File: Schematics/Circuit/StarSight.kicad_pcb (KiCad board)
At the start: 2 copper layers, 21 parts, among them J10 IR1, J11 IR1, J12 ultSound1, J13 ultSound1, J14 ultSound1, J15 ultSound1, J2 Line1, J3 Line2, J4 Line3, J5 Line4, J6 Line5, J7 IR1, J8 IR1, J9 IR1, P1 CONN_13X2, P2 Power, U1 LM1084IT-5.0/NOPB

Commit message: Fix pcb
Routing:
- added copper zone on F.Cu, net GND

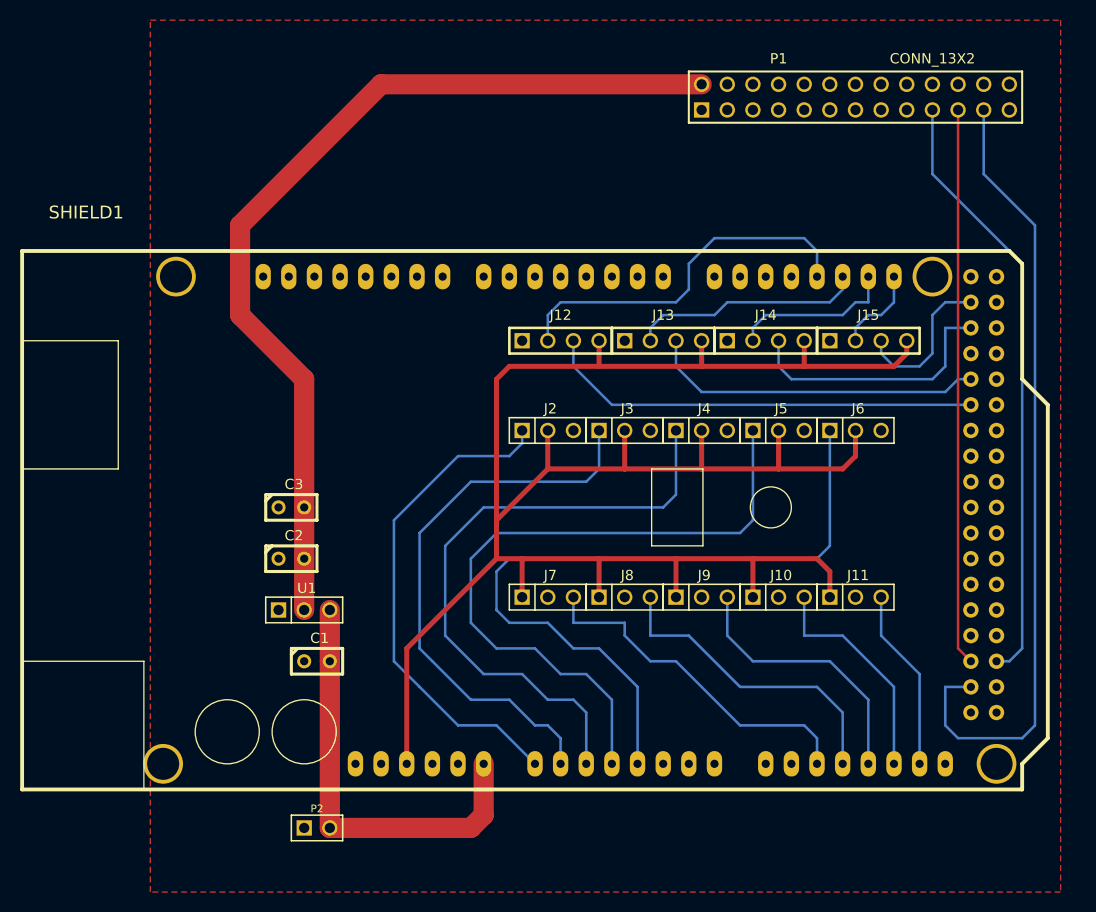
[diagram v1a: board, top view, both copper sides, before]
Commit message: Edit board - remove drivers, add pins
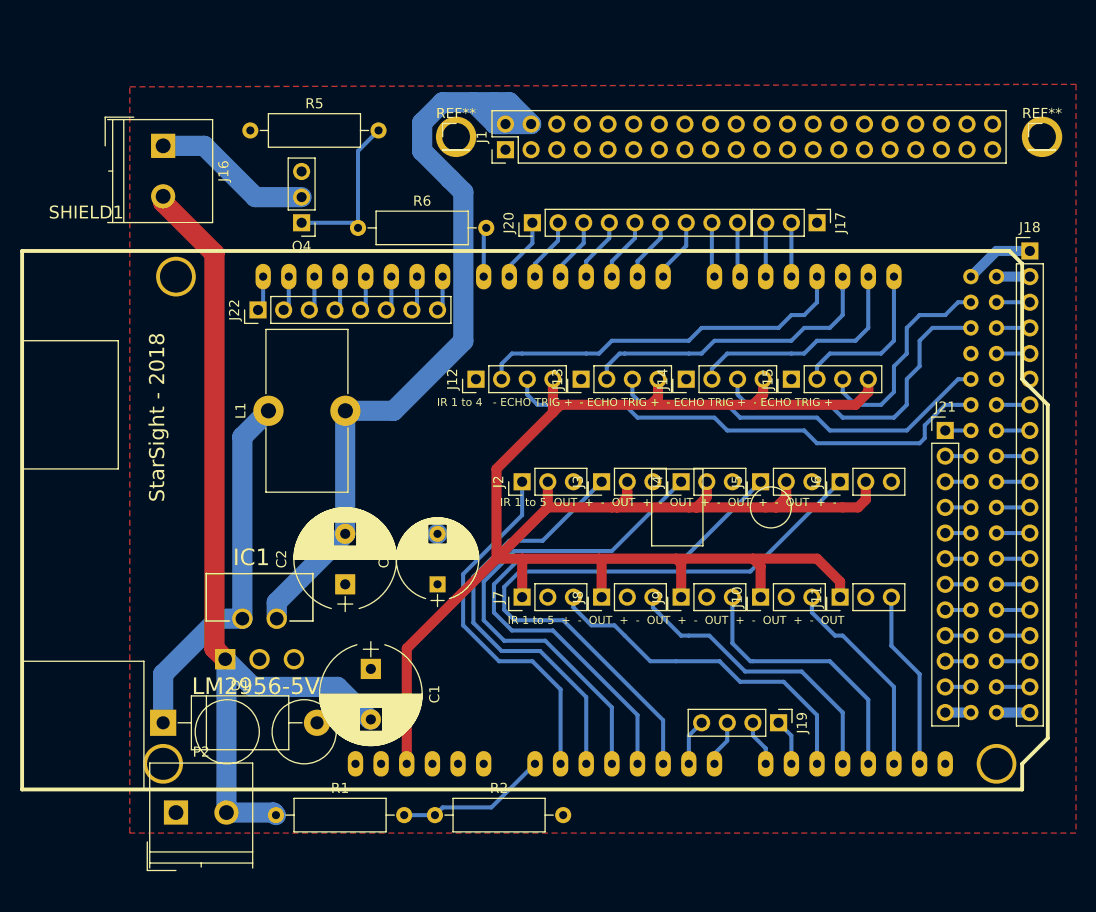
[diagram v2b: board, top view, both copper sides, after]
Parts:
- removed P1: CONN_13X2, pin_array_13x2
- removed U1: LM1084IT-5.0/NOPB, PIN_ARRAY_3X1
- added D1: 1n5824, Diodes_THT:D_DO-201_P15.24mm_Horizontal, F.Cu at (116.8, 111.5)
- added IC1: LM2956-5V, reg:TO170P470X1016X2092-5P, F.Cu at (129.8, 93.0)
- added J1: Conn_02x20_Odd_Even, Pin_Headers:Pin_Header_Straight_2x20_Pitch2.54mm, F.Cu at (150.7, 54.7)
- added J16: Conn_01x02, Connectors_Terminal_Blocks:TerminalBlock_Philmore_TB132_02x5mm_Straight, F.Cu at (116.8, 54.4)
- added J17: Conn_01x03, Pin_Headers:Pin_Header_Straight_1x03_Pitch2.54mm, F.Cu at (181.6, 62.0)
- added J18: Conn_01x19, Pin_Headers:Pin_Header_Straight_1x19_Pitch2.54mm, F.Cu at (202.7, 64.8)
- added J19: Conn_01x04, Pin_Headers:Pin_Header_Straight_1x04_Pitch2.54mm, F.Cu at (177.8, 111.5)
- added J20: Conn_01x09, Pin_Headers:Pin_Header_Straight_1x09_Pitch2.54mm, F.Cu at (153.4, 62.0)
- added J21: Conn_01x12, Pin_Headers:Pin_Header_Straight_1x12_Pitch2.54mm, F.Cu at (194.3, 82.5)
- added J22: Conn_01x08, Pin_Headers:Pin_Header_Straight_1x08_Pitch2.54mm, F.Cu at (126.2, 70.6)
- added L1: 33 uH, Inductors_THT:L_Toroid_Vertical_L16.0mm_W8.0mm_P7.62mm, F.Cu at (127.3, 80.6)
- added Q4: BUZZ TO220, Pin_Headers:Pin_Header_Straight_1x03_Pitch2.54mm, F.Cu at (130.6, 62.0)
- added R1: 20k, Resistors_THT:R_Axial_DIN0309_L9.0mm_D3.2mm_P12.70mm_Horizontal, F.Cu at (128.0, 120.7)
- added R2: 10k, Resistors_THT:R_Axial_DIN0309_L9.0mm_D3.2mm_P12.70mm_Horizontal, F.Cu at (143.8, 120.7)
- added R5: 10k, Resistors_THT:R_Axial_DIN0309_L9.0mm_D3.2mm_P12.70mm_Horizontal, F.Cu at (125.5, 52.8)
- added R6: 100, Resistors_THT:R_Axial_DIN0309_L9.0mm_D3.2mm_P12.70mm_Horizontal, F.Cu at (136.1, 62.5)
- added REF**: Pin_Header_Straight_1x01_Pitch2.54mm, Pin_Headers:Pin_Header_Straight_1x01_Pitch2.54mm, F.Cu at (203.9, 53.5)
- added REF**: Pin_Header_Straight_1x01_Pitch2.54mm, Pin_Headers:Pin_Header_Straight_1x01_Pitch2.54mm, F.Cu at (145.9, 53.5)
- C1: value 10 uF -> 220 uF; footprint C1 -> Capacitors_THT:CP_Radial_D10.0mm_P5.00mm
- C2: value 10 uF -> 680 uF; footprint C1 -> Capacitors_THT:CP_Radial_D10.0mm_P5.00mm
- C3: footprint C1 -> Capacitors_THT:CP_Radial_D8.0mm_P5.00mm
- J10, J11, J2, J3, J4, J5, J6, J7, J8, J9: footprint PIN_ARRAY_3X1 -> Pin_Headers:Pin_Header_Straight_1x03_Pitch2.54mm
- J12, J13, J14, J15: footprint PIN_ARRAY_4x1 -> Pin_Headers:Pin_Header_Straight_1x04_Pitch2.54mm
- P2: footprint PIN_ARRAY_2X1 -> Connectors_Terminal_Blocks:TerminalBlock_Philmore_TB132_02x5mm_Straight
- SHIELD1: footprint ARDUINO_MEGA_SHIELD -> arduino_shields:ARDUINO_MEGA_SHIELD
- moved C3 16.4 mm to (144.0, 97.8), turned to 90 degrees
- moved P2 14.1 mm to (118.1, 120.4)
- moved J12 9.21 mm to (147.8, 77.5), turned to 90 degrees
- moved J13 8.98 mm to (158.2, 77.5), turned to 90 degrees
- moved J14 8.75 mm to (168.7, 77.5), turned to 90 degrees
- moved J15 8.52 mm to (179.1, 77.5), turned to 90 degrees
- moved C2 5.91 mm to (134.9, 97.8), turned to 90 degrees
- moved J2 5.68 mm to (152.4, 87.6), turned to 90 degrees
- moved J3 5.57 mm to (160.3, 87.6), turned to 90 degrees
- moved J4 5.47 mm to (168.1, 87.6), turned to 90 degrees
- moved C1 5.39 mm to (137.4, 106.2), turned to 270 degrees
- moved J5 5.38 mm to (176.0, 87.6), turned to 90 degrees
- moved J6 5.30 mm to (183.9, 87.6), turned to 90 degrees
- moved J7 2.54 mm to (152.4, 99.1), turned to 90 degrees
- moved J8 2.29 mm to (160.3, 99.1), turned to 90 degrees
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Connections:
- C1 pad 2: N-0000085 -> +12V
- C2 pad 2: N-0000086 -> +5V
- C3 pad 2: N-0000086 -> +5V
- J2 pad 1: N-0000022 -> Net-(J2-Pad1)
- J3 pad 1: N-0000028 -> Net-(J3-Pad1)
- J4 pad 1: N-0000029 -> Net-(J4-Pad1)
- J5 pad 1: N-0000030 -> Net-(J5-Pad1)
- J6 pad 1: N-0000011 -> Net-(J6-Pad1)
- P2 pad 2: N-0000085 -> +12V
- SHIELD1 pad 0: (no net) -> Net-(J20-Pad7)
- SHIELD1 pad 1: (no net) -> Net-(J20-Pad6)
- SHIELD1 pad 10: (no net) -> Net-(J22-Pad6)
- SHIELD1 pad 11: (no net) -> Net-(J22-Pad5)
- SHIELD1 pad 12: (no net) -> Net-(J22-Pad4)
- SHIELD1 pad 13: (no net) -> Net-(J22-Pad3)
- SHIELD1 pad 14: (no net) -> Net-(J20-Pad8)
- SHIELD1 pad 15: (no net) -> Net-(J20-Pad9)
- SHIELD1 pad 16: (no net) -> /TX
- SHIELD1 pad 17: (no net) -> /RX
- SHIELD1 pad 2: (no net) -> Net-(J20-Pad5)
- SHIELD1 pad 23: (no net) -> Net-(J18-Pad3)
- SHIELD1 pad 25: (no net) -> Net-(J18-Pad4)
- SHIELD1 pad 27: (no net) -> Net-(J18-Pad5)
- SHIELD1 pad 29: (no net) -> Net-(J18-Pad6)
- SHIELD1 pad 3: (no net) -> Net-(J20-Pad4)
- SHIELD1 pad 31: (no net) -> Net-(J18-Pad7)
- SHIELD1 pad 32: (no net) -> Net-(J21-Pad1)
- SHIELD1 pad 33: (no net) -> Net-(J18-Pad8)
- SHIELD1 pad 34: (no net) -> Net-(J21-Pad2)
- SHIELD1 pad 35: (no net) -> Net-(J18-Pad9)
- SHIELD1 pad 36: (no net) -> Net-(J21-Pad3)
- SHIELD1 pad 37: (no net) -> Net-(J18-Pad10)
- SHIELD1 pad 38: (no net) -> Net-(J21-Pad4)
- SHIELD1 pad 39: (no net) -> Net-(J18-Pad11)
- SHIELD1 pad 4: (no net) -> Net-(J20-Pad3)
- SHIELD1 pad 40: (no net) -> Net-(J21-Pad5)
- SHIELD1 pad 41: (no net) -> Net-(J18-Pad12)
- SHIELD1 pad 42: (no net) -> Net-(J21-Pad6)
- SHIELD1 pad 43: (no net) -> Net-(J18-Pad13)
- SHIELD1 pad 44: (no net) -> Net-(J21-Pad7)
- SHIELD1 pad 45: (no net) -> Net-(J18-Pad14)
- SHIELD1 pad 46: (no net) -> Net-(J21-Pad8)
- SHIELD1 pad 47: (no net) -> Net-(J18-Pad15)
- SHIELD1 pad 48: (no net) -> Net-(J21-Pad9)
- SHIELD1 pad 49: (no net) -> Net-(J18-Pad16)
- SHIELD1 pad 5: (no net) -> Net-(J20-Pad2)
- SHIELD1 pad 50: /GPIO9(MISO) -> Net-(J21-Pad10)
- SHIELD1 pad 51: /GPIO10(MOSI) -> Net-(J18-Pad17)
- SHIELD1 pad 52: /GPIO11(SCLK) -> Net-(J21-Pad11)
- SHIELD1 pad 53: (no net) -> Net-(J18-Pad18)
- SHIELD1 pad 5V_4: (no net) -> Net-(J18-Pad1)
- SHIELD1 pad 5V_5: (no net) -> Net-(J18-Pad2)
- SHIELD1 pad 6: (no net) -> Net-(J20-Pad1)
- SHIELD1 pad 7: (no net) -> Net-(R6-Pad2)
- SHIELD1 pad 8: (no net) -> Net-(J22-Pad8)
- SHIELD1 pad 9: (no net) -> Net-(J22-Pad7)
- SHIELD1 pad AD0: N-0000022 -> /V_READ
- SHIELD1 pad AD1: N-0000028 -> Net-(J2-Pad1)
- SHIELD1 pad AD2: N-0000029 -> Net-(J3-Pad1)
- SHIELD1 pad AD3: N-0000030 -> Net-(J4-Pad1)
- SHIELD1 pad AD4: N-0000011 -> Net-(J5-Pad1)
- SHIELD1 pad AD5: (no net) -> Net-(J6-Pad1)
- SHIELD1 pad AD6: (no net) -> Net-(J19-Pad4)
- SHIELD1 pad AD7: (no net) -> Net-(J19-Pad3)
- SHIELD1 pad AD8: (no net) -> Net-(J19-Pad2)
- SHIELD1 pad AD9: (no net) -> Net-(J19-Pad1)
- SHIELD1 pad AREF: (no net) -> Net-(J22-Pad1)
- SHIELD1 pad GND1: (no net) -> Net-(SHIELD1-PadGND1)
- SHIELD1 pad GND3: (no net) -> Net-(J22-Pad2)
- SHIELD1 pad GND4: (no net) -> Net-(J21-Pad12)
- SHIELD1 pad GND5: (no net) -> Net-(J18-Pad19)
- SHIELD1 pad V_IN: N-0000085 -> (no net)
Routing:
- net N-0000086: track 92.2 -> 0.00 mm
- net +12V: track 0.00 -> 85.5 mm
- net /GPIO11(SCLK): track 79.4 -> 0.00 mm
- net N-0000011: track 74.1 -> 0.00 mm
- net +5V: track 199.7 -> 271.9 mm
- net N-0000030: track 68.2 -> 0.00 mm
- net Net-(J6-Pad1): track 0.00 -> 64.5 mm
- net N-0000029: track 62.4 -> 0.00 mm
- net /GPIO10(MOSI): track 60.1 -> 0.00 mm
- net Net-(J5-Pad1): track 0.00 -> 56.7 mm
- net N-0000028: track 55.8 -> 0.00 mm
- net /GPIO9(MISO): track 55.1 -> 0.00 mm
- net Net-(J4-Pad1): track 0.00 -> 49.3 mm
- net N-0000022: track 49.3 -> 0.00 mm
- net N-0000085: track 42.4 -> 0.00 mm
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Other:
- board text added: "IR 1 to 4 - ECHO TRIG + - ECHO TRIG + - ECHO TRIG + - ECHO TRIG +"
- board text added: "IR 1 to 5 + - OUT + - OUT + - OUT + - OUT + - OUT"
- board text added: "IR 1 to 5 OUT + - OUT + - OUT + - OUT + - OUT + -"
- board text added: "StarSight - 2018"
